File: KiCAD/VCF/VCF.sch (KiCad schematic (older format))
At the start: 52 parts, among them J1 Power, J2 MJ-3502, J3 MJ-3502, J4 MJ-3502, Q1 2N3906, Q10 2N3392, Q11 2N3392, Q12 2N3392, Q2 2N3392, Q3 2N3392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

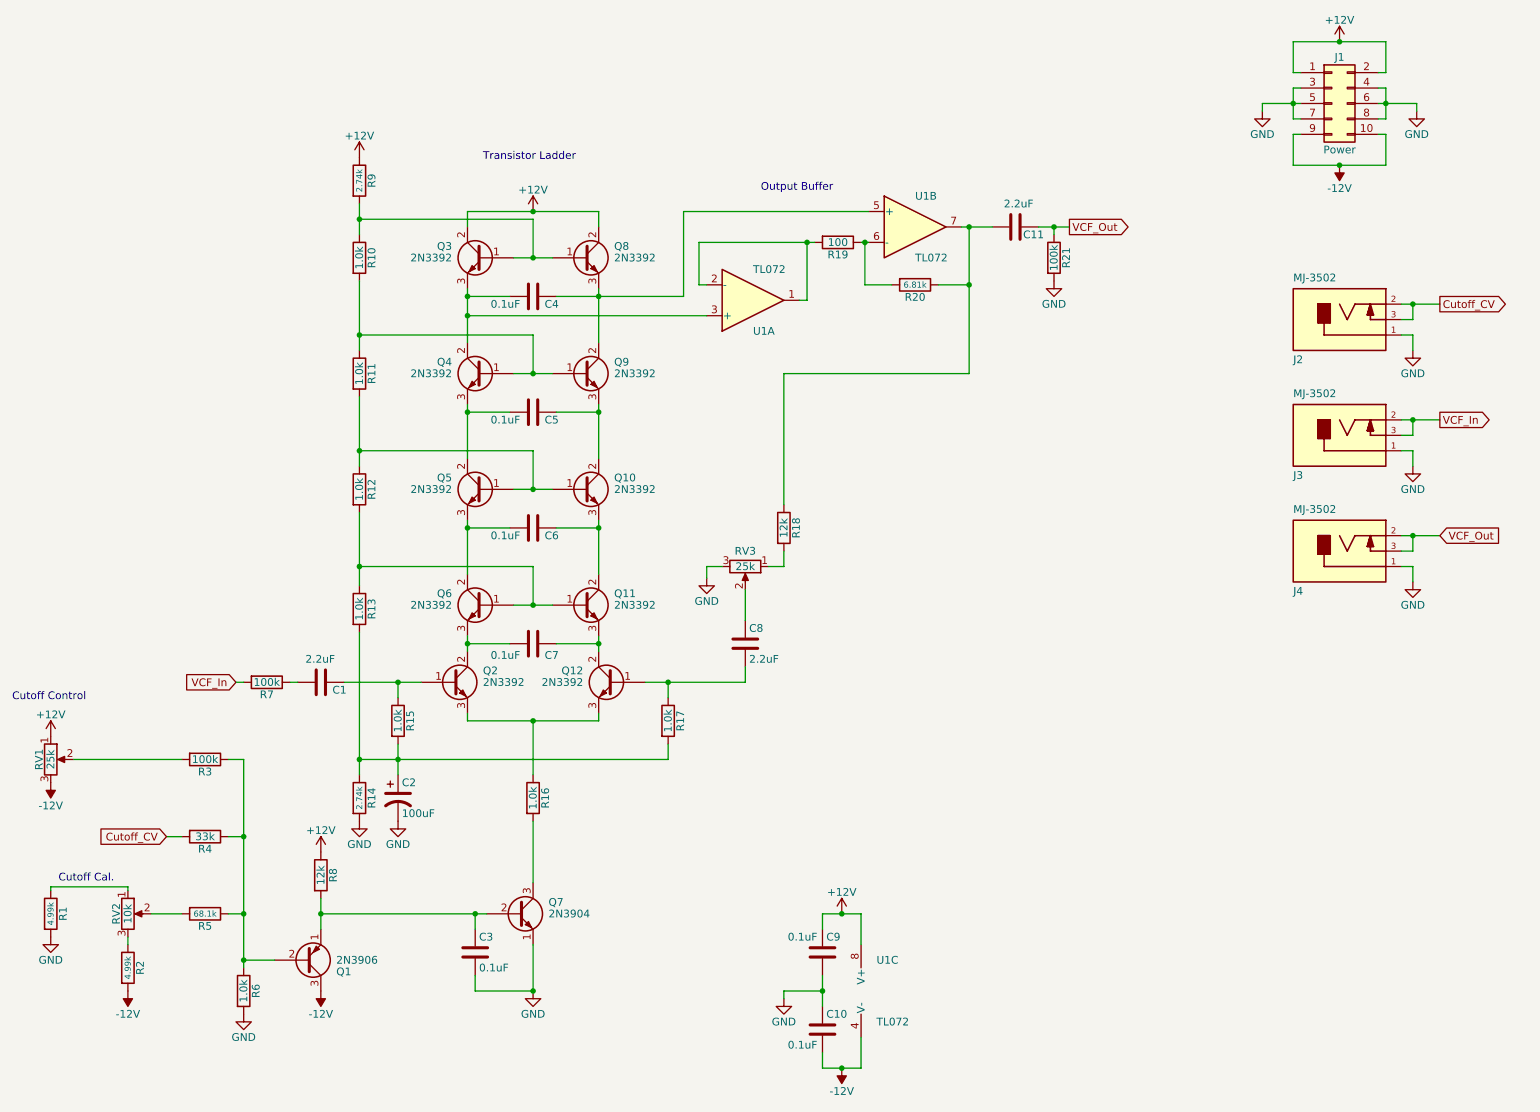
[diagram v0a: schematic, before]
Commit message: added voltage regulator to VCF
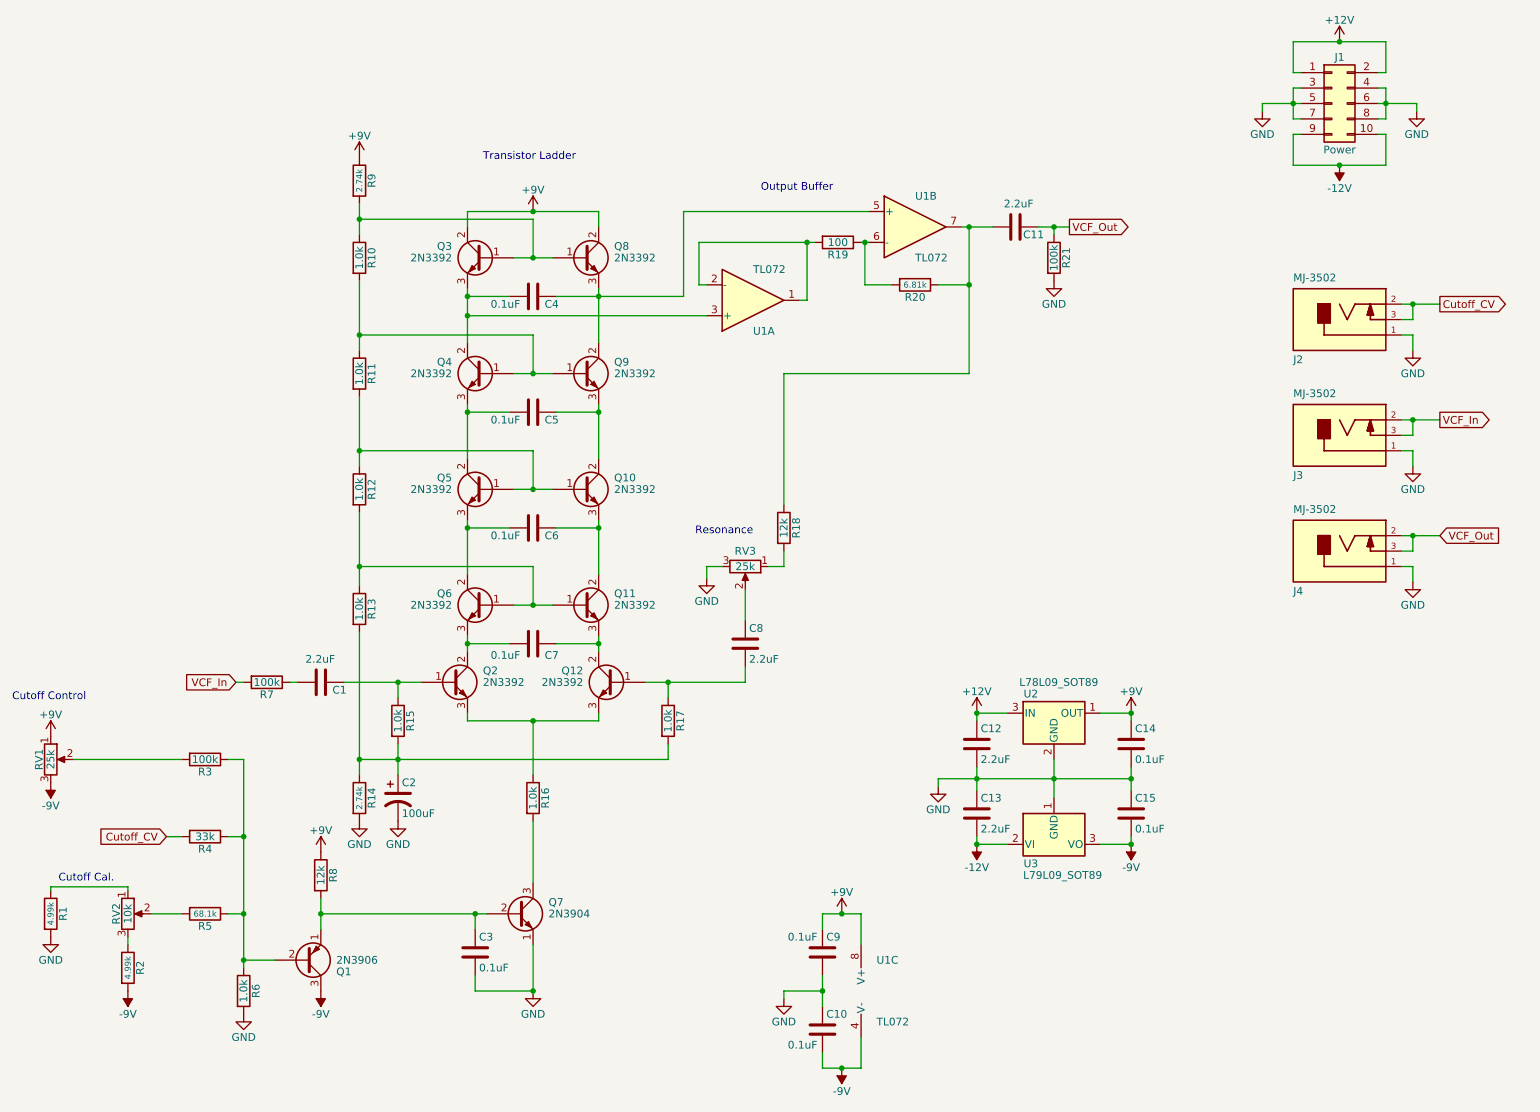
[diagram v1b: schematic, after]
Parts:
- added C12, C13: 2.2uF, Synth:C_1206, symbol Device:C
- added C14, C15: 0.1uF, Synth:C_1206, symbol Device:C
- added U2: L78L09_SOT89, Package_TO_SOT_SMD:SOT-89-3, symbol Regulator_Linear:L78L09_SOT89
- added U3: L79L09_SOT89, Package_TO_SOT_SMD:SOT-89-3, symbol Regulator_Linear:L79L05_SOT89
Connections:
- net +12V: now also C12.1, U2.3 (IN); no longer C9.1, Q3.2 (C), Q8.2 (C), R8.1, R9.1, RV1.1, U1.8 (V+)
- net -12V: now also C13.2, U3.2 (VI); no longer C10.2, Q1.3 (C), R2.2, RV1.3, U1.4 (V-)
- net GND: now also C12.2, C13.1, C14.2, C15.1, U2.2 (GND), U3.1 (GND)
- new net +9V: C14.1, C9.1, Q3.2 (C), Q8.2 (C), R8.1, R9.1, RV1.1, U1.8 (V+), U2.1 (OUT)
- new net -9V: C10.2, C15.2, Q1.3 (C), R2.2, RV1.3, U1.4 (V-), U3.3 (VO)
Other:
- note added: "Resonance"
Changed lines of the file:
@@
 	3700 2050 3700 1950
 Wire Wire Line
-	3700 1950 4125 1950
-Wire Wire Line
 	4550 1950 4550 2050
-$Comp
-L power:+12V #PWR011
-U 1 1 5CD832C2
-P 4125 1950
-F 0 "#PWR011" H 4125 1800 50  0001 C CNN
-F 1 "+12V" H 4125 2090 50  0000 C CNN
-F 2 "" H 4125 1950 50  0001 C CNN
-F 3 "" H 4125 1950 50  0001 C CNN
-	1    4125 1950
-	1    0    0    -1
-$EndComp
-Connection ~ 4125 1950
-Wire Wire Line
-	4125 1950 4550 1950
 $Comp
 L Device:R R10
@@
 Wire Wire Line
 	3000 4250 3000 3900
-$Comp
-L power:+12V #PWR08
-U 1 1 5CD8AF4F
-P 3000 1600
-F 0 "#PWR08" H 3000 1450 50  0001 C CNN
-F 1 "+12V" H 3000 1740 50  0000 C CNN
-F 2 "" H 3000 1600 50  0001 C CNN
-F 3 "" H 3000 1600 50  0001 C CNN
-	1    3000 1600
-	1    0    0    -1
-$EndComp
 $Comp
 L Synth:2N3392 Q2
@@
 	1    0    0    -1
 $EndComp
-$Comp
-L power:-12V #PWR07
-U 1 1 5CDA8A41
-P 2750 7000
-F 0 "#PWR07" H 2750 7100 50  0001 C CNN
-F 1 "-12V" H 2750 7150 50  0000 C CNN
-F 2 "" H 2750 7000 50  0001 C CNN
-F 3 "" H 2750 7000 50  0001 C CNN
-	1    2750 7000
-	-1   0    0    1
-$EndComp
-$Comp
-L power:+12V #PWR06
-U 1 1 5CDA9576
-P 2750 6100
-F 0 "#PWR06" H 2750 5950 50  0001 C CNN
-F 1 "+12V" H 2750 6240 50  0000 C CNN
-F 2 "" H 2750 6100 50  0001 C CNN
-F 3 "" H 2750 6100 50  0001 C CNN
-	1    2750 6100
-	1    0    0    -1
-$EndComp
 Wire Wire Line
 	2750 6400 2750 6500
@@
 $EndComp
 $Comp
-L power:-12V #PWR04
-U 1 1 5CDBCA88
-P 1500 7000
-F 0 "#PWR04" H 1500 7100 50  0001 C CNN
-F 1 "-12V" H 1500 7150 50  0000 C CNN
-F 2 "" H 1500 7000 50  0001 C CNN
-F 3 "" H 1500 7000 50  0001 C CNN
-	1    1500 7000
-	-1   0    0    1
-$EndComp
-$Comp
 L power:GND #PWR03
 U 1 1 5CDBE0D1
@@
 F 3 "~" H 1000 5500 50  0001 C CNN
 	1    1000 5500
-	1    0    0    -1
-$EndComp
-$Comp
-L power:-12V #PWR02
-U 1 1 5CDCFF1F
-P 1000 5650
-F 0 "#PWR02" H 1000 5750 50  0001 C CNN
-F 1 "-12V" H 1000 5800 50  0000 C CNN
-F 2 "" H 1000 5650 50  0001 C CNN
-F 3 "" H 1000 5650 50  0001 C CNN
-	1    1000 5650
-	-1   0    0    1
-$EndComp
-$Comp
-L power:+12V #PWR01
-U 1 1 5CDD0479
-P 1000 5350
-F 0 "#PWR01" H 1000 5200 50  0001 C CNN
-F 1 "+12V" H 1000 5490 50  0000 C CNN
-F 2 "" H 1000 5350 50  0001 C CNN
-F 3 "" H 1000 5350 50  0001 C CNN
-	1    1000 5350
 	1    0    0    -1
 $EndComp
@@
 	6250 6700 6250 6500
 Wire Wire Line
-	6250 6500 6125 6500
-Wire Wire Line
 	6000 6500 6000 6600
 Wire Wire Line
 	6250 7300 6250 7500
-Wire Wire Line
-	6250 7500 6125 7500
 Wire Wire Line
 	6000 7500 6000 7400
@@
 	1    0    0    -1
 $EndComp
-$Comp
-L power:-12V #PWR016
-U 1 1 5CE4AA22
-P 6125 7500
-F 0 "#PWR016" H 6125 7600 50  0001 C CNN
-F 1 "-12V" H 6125 7650 50  0000 C CNN
-F 2 "" H 6125 7500 50  0001 C CNN
-F 3 "" H 6125 7500 50  0001 C CNN
-	1    6125 7500
-	-1   0    0    1
-$EndComp
-Connection ~ 6125 7500
-Wire Wire Line
-	6125 7500 6000 7500
-$Comp
-L power:+12V #PWR015
-U 1 1 5CE4B4FD
-P 6125 6500
-F 0 "#PWR015" H 6125 6350 50  0001 C CNN
-F 1 "+12V" H 6125 6640 50  0000 C CNN
-F 2 "" H 6125 6500 50  0001 C CNN
-F 3 "" H 6125 6500 50  0001 C CNN
-	1    6125 6500
-	1    0    0    -1
-$EndComp
-Connection ~ 6125 6500
-Wire Wire Line
-	6125 6500 6000 6500
 Wire Wire Line
 	5750 7050 5750 7000
@@
 Text Notes 5600 1825 0    50   ~ 0
 Output Buffer
+Text Notes 5175 4050 0    50   ~ 0
+Resonance
+$Comp
+L power:-9V #PWR02
+U 1 1 5CD8390B
+P 1000 5650
+F 0 "#PWR02" H 1000 5525 50  0001 C CNN
+F 1 "-9V" H 1000 5800 50  0000 C CNN
+F 2 "" H 1000 5650 50  0001 C CNN
+F 3 "" H 1000 5650 50  0001 C CNN
+	1    1000 5650
+	-1   0    0    1
+$EndComp
+$Comp
+L power:-9V #PWR04
+U 1 1 5CD84903
+P 1500 7000
+F 0 "#PWR04" H 1500 6875 50  0001 C CNN
+F 1 "-9V" H 1500 7150 50  0000 C CNN
+F 2 "" H 1500 7000 50  0001 C CNN
+F 3 "" H 1500 7000 50  0001 C CNN
+	1    1500 7000
+	-1   0    0    1
+$EndComp
+$Comp
+L power:-9V #PWR07
+U 1 1 5CD85727
+P 2750 7000
+F 0 "#PWR07" H 2750 6875 50  0001 C CNN
+F 1 "-9V" H 2750 7150 50  0000 C CNN
+F 2 "" H 2750 7000 50  0001 C CNN
+F 3 "" H 2750 7000 50  0001 C CNN
+	1    2750 7000
+	-1   0    0    1
+$EndComp
+Wire Wire Line
+	6000 7500 6125 7500
+$Comp
+L power:-9V #PWR016
+U 1 1 5CD86207
+P 6125 7500
+F 0 "#PWR016" H 6125 7375 50  0001 C CNN
+F 1 "-9V" H 6125 7650 50  0000 C CNN
+F 2 "" H 6125 7500 50  0001 C CNN
+F 3 "" H 6125 7500 50  0001 C CNN
+	1    6125 7500
+	-1   0    0    1
+$EndComp
+Connection ~ 6125 7500
+Wire Wire Line
+	6125 7500 6250 7500
+Wire Wire Line
+	6000 6500 6125 6500
+$Comp
+L power:+9V #PWR015
+U 1 1 5CD87CB2
+P 6125 6500
+F 0 "#PWR015" H 6125 6350 50  0001 C CNN
+F 1 "+9V" H 6125 6640 50  0000 C CNN
+F 2 "" H 6125 6500 50  0001 C CNN
+F 3 "" H 6125 6500 50  0001 C CNN
+	1    6125 6500
+	1    0    0    -1
+$EndComp
+Connection ~ 6125 6500
+Wire Wire Line
+	6125 6500 6250 6500
+$Comp
+L power:+9V #PWR06
+U 1 1 5CD88F36
+P 2750 6100
+F 0 "#PWR06" H 2750 5950 50  0001 C CNN
+F 1 "+9V" H 2750 6240 50  0000 C CNN
+F 2 "" H 2750 6100 50  0001 C CNN
+F 3 "" H 2750 6100 50  0001 C CNN
+	1    2750 6100
+	1    0    0    -1
+$EndComp
+$Comp
+L power:+9V #PWR01
+U 1 1 5CD8926C
+P 1000 5350
+F 0 "#PWR01" H 1000 5200 50  0001 C CNN
+F 1 "+9V" H 1000 5490 50  0000 C CNN
+F 2 "" H 1000 5350 50  0001 C CNN
+F 3 "" H 1000 5350 50  0001 C CNN
+	1    1000 5350
+	1    0    0    -1
+$EndComp
+Wire Wire Line
+	3700 1950 4125 1950
+$Comp
+L power:+9V #PWR011
+U 1 1 5CD89C02
+P 4125 1950
+F 0 "#PWR011" H 4125 1800 50  0001 C CNN
+F 1 "+9V" H 4125 2090 50  0000 C CNN
+F 2 "" H 4125 1950 50  0001 C CNN
+F 3 "" H 4125 1950 50  0001 C CNN
+	1    4125 1950
+	1    0    0    -1
+$EndComp
+Connection ~ 4125 1950
+Wire Wire Line
+	4125 1950 4550 1950
+$Comp
+L power:+9V #PWR08
+U 1 1 5CD8A66D
+P 3000 1600
+F 0 "#PWR08" H 3000 1450 50  0001 C CNN
+F 1 "+9V" H 3000 1740 50  0000 C CNN
+F 2 "" H 3000 1600 50  0001 C CNN
+F 3 "" H 3000 1600 50  0001 C CNN
+	1    3000 1600
+	1    0    0    -1
+$EndComp
+$Comp
+L Device:C C15
+U 1 1 5CD8F91E
+P 8000 5850
+F 0 "C15" H 8025 5950 50  0000 L CNN
+F 1 "0.1uF" H 8025 5750 50  0000 L CNN
+F 2 "Synth:C_1206" H 8038 5700 50  0001 C CNN
+F 3 "~" H 8000 5850 50  0001 C CNN
+	1    8000 5850
+	1    0    0    -1
+$EndComp
+$Comp
+L Device:C C14
+U 1 1 5CD90EFA
+P 8000 5400
+F 0 "C14" H 8025 5500 50  0000 L CNN
+F 1 "0.1uF" H 8025 5300 50  0000 L CNN
+F 2 "Synth:C_1206" H 8038 5250 50  0001 C CNN
+F 3 "~" H 8000 5400 50  0001 C CNN
+	1    8000 5400
+	1    0    0    -1
+$EndComp
+$Comp
+L Device:C C12
+U 1 1 5CD923FA
+P 7000 5400
+F 0 "C12" H 7025 5500 50  0000 L CNN
+F 1 "2.2uF" H 7025 5300 50  0000 L CNN
+F 2 "Synth:C_1206" H 7038 5250 50  0001 C CNN
+F 3 "~" H 7000 5400 50  0001 C CNN
+	1    7000 5400
+	1    0    0    -1
+$EndComp
+$Comp
+L Device:C C13
+U 1 1 5CD93424
+P 7000 5850
+F 0 "C13" H 7025 5950 50  0000 L CNN
+F 1 "2.2uF" H 7025 5750 50  0000 L CNN
+F 2 "Synth:C_1206" H 7038 5700 50  0001 C CNN
+F 3 "~" H 7000 5850 50  0001 C CNN
+	1    7000 5850
+	1    0    0    -1
+$EndComp
+Wire Wire Line
+	7500 5500 7500 5625
+Wire Wire Line
+	7800 6050 8000 6050
+Wire Wire Line
+	8000 6050 8000 6000
+Wire Wire Line
+	7200 6050 7000 6050
+Wire Wire Line
+	7000 6050 7000 6000
+Wire Wire Line
+	7000 5550 7000 5625
+Wire Wire Line
+	7000 5250 7000 5200
+Wire Wire Line
+	7000 5200 7200 5200
+Wire Wire Line
+	7800 5200 8000 5200
+Wire Wire Line
+	8000 5200 8000 5250
+Wire Wire Line
+	8000 5550 8000 5625
+Wire Wire Line
+	7000 5625 7500 5625
+Connection ~ 7000 5625
+Wire Wire Line
+	7000 5625 7000 5700
+Connection ~ 7500 5625
+Wire Wire Line
+	7500 5625 7500 5750
+Wire Wire Line
+	7500 5625 8000 5625
+Connection ~ 8000 5625
+Wire Wire Line
+	8000 5625 8000 5700
+$Comp
+L power:+9V #PWR028
+U 1 1 5CDE2F3A
+P 8000 5200
+F 0 "#PWR028" H 8000 5050 50  0001 C CNN
+F 1 "+9V" H 8000 5340 50  0000 C CNN
+F 2 "" H 8000 5200 50  0001 C CNN
+F 3 "" H 8000 5200 50  0001 C CNN
+	1    8000 5200
+	1    0    0    -1
+$EndComp
+Connection ~ 8000 5200
+$Comp
+L power:-9V #PWR029
+U 1 1 5CDE5370
+P 8000 6050
+F 0 "#PWR029" H 8000 5925 50  0001 C CNN
+F 1 "-9V" H 8000 6200 50  0000 C CNN
+F 2 "" H 8000 6050 50  0001 C CNN
+F 3 "" H 8000 6050 50  0001 C CNN
+	1    8000 6050
+	-1   0    0    1
+$EndComp
+Connection ~ 8000 6050
+$Comp
+L power:+12V #PWR026
+U 1 1 5CDE5D8C
+P 7000 5200
+F 0 "#PWR026" H 7000 5050 50  0001 C CNN
+F 1 "+12V" H 7000 5340 50  0000 C CNN
+F 2 "" H 7000 5200 50  0001 C CNN
+F 3 "" H 7000 5200 50  0001 C CNN
+	1    7000 5200
+	1    0    0    -1
+$EndComp
+Connection ~ 7000 5200
+$Comp
+L power:-12V #PWR027
+U 1 1 5CDE7466
+P 7000 6050
+F 0 "#PWR027" H 7000 6150 50  0001 C CNN
+F 1 "-12V" H 7000 6200 50  0000 C CNN
+F 2 "" H 7000 6050 50  0001 C CNN
+F 3 "" H 7000 6050 50  0001 C CNN
+	1    7000 6050
+	-1   0    0    1
+$EndComp
+Connection ~ 7000 6050
+$Comp
+L power:GND #PWR025
+U 1 1 5CDE7DB0
+P 6750 5675
+F 0 "#PWR025" H 6750 5425 50  0001 C CNN
+F 1 "GND" H 6750 5525 50  0000 C CNN
+F 2 "" H 6750 5675 50  0001 C CNN
+F 3 "" H 6750 5675 50  0001 C CNN
+	1    6750 5675
+	1    0    0    -1
+$EndComp
+Wire Wire Line
+	6750 5675 6750 5625
+Wire Wire Line
+	6750 5625 7000 5625
+$Comp
+L Regulator_Linear:L78L09_SOT89 U2
+U 1 1 5CDF2F61
+P 7500 5200
+F 0 "U2" H 7350 5325 50  0000 C CNN
+F 1 "L78L09_SOT89" H 7275 5400 50  0000 L CNN
+F 2 "Package_TO_SOT_SMD:SOT-89-3" H 7500 5400 50  0001 C CIN
+F 3 "http://www.st.com/content/ccc/resource/technical/document/datasheet/15/55/e5/aa/23/5b/43/fd/CD00000446.pdf/files/CD00000446.pdf/jcr:content/translations/en.CD00000446.pdf" H 7500 5150 50  0001 C CNN
+	1    7500 5200
+	1    0    0    -1
+$EndComp
+$Comp
+L Regulator_Linear:L79L05_SOT89 U3
+U 1 1 5CDF4B2F
+P 7500 6050
+F 0 "U3" H 7350 5925 50  0000 C CNN
+F 1 "L79L09_SOT89" H 7300 5850 50  0000 L CNN
+F 2 "Package_TO_SOT_SMD:SOT-89-3" H 7500 5850 50  0001 C CIN
+F 3 "http://www.farnell.com/datasheets/1827870.pdf" H 7500 6050 50  0001 C CNN
+	1    7500 6050
+	1    0    0    -1
+$EndComp
 $EndSCHEMATC
